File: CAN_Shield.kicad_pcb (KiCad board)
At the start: 2 copper layers, 65 x 56.5 mm, 22 parts, among them J1 GPIO, J2 KF128-2.54-4P, U1 MX128-5.08-09P-GN01-CU-Y-A, U2 MCP2515T-I/SO, U4 SN65HVD230DR, X1 X322516MLB4SI

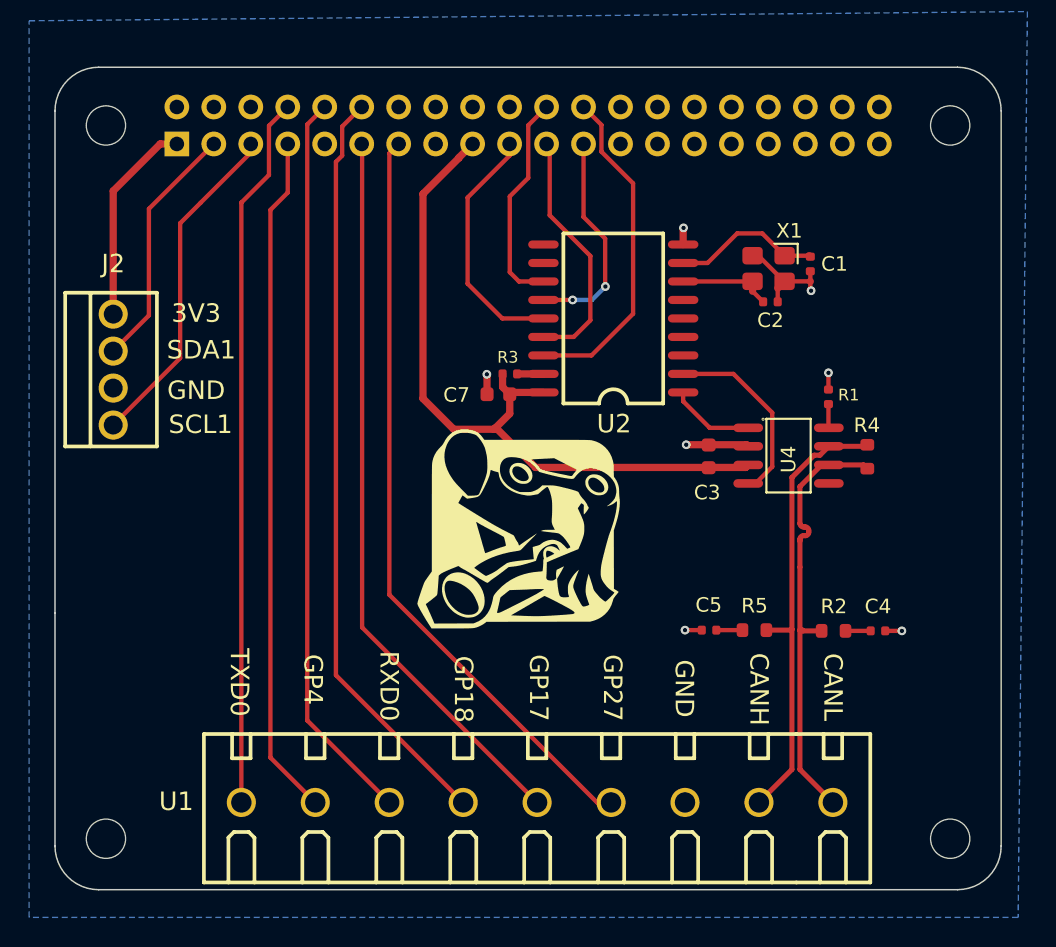
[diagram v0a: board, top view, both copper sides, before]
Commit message: finished schematics and layout for 3 terminal block except CAN
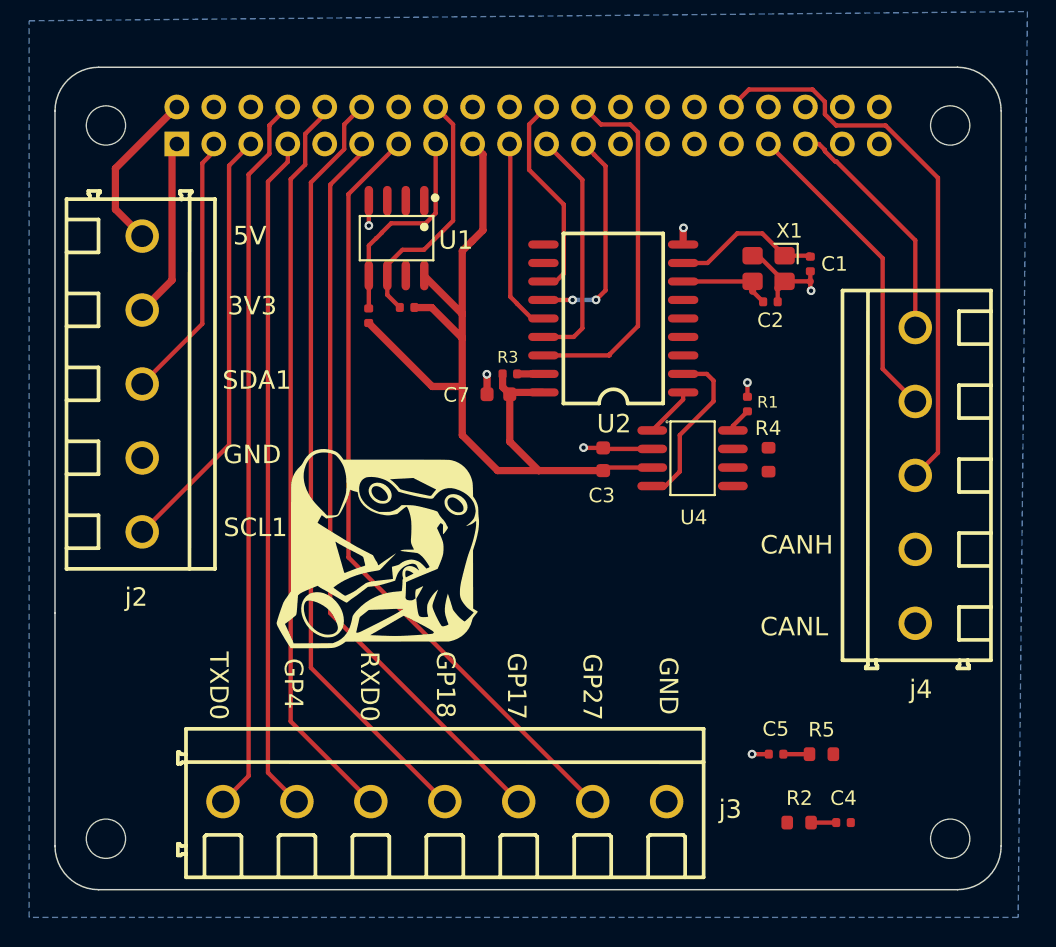
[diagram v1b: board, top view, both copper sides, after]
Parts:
- removed J2: KF128-2.54-4P, ImportFP:CONN-TH_4P-P2.54_KF128-2.54-4P
- added R6: 4.7kΩ, PCM_JLCPCB:R_0402, F.Cu at (124.2, 60.0)
- added R7: 4.7kΩ, PCM_JLCPCB:R_0402, F.Cu at (121.5, 60.6)
- added j2: DB128V-5.08-5P-GN-S, ImportFP:CONN-TH_5P-P5.08_DIBO_DB128V-5.08-5P-GN-S, F.Cu at (106.0, 65.3)
- added j3: DB128V-5.08-7P-GN-S, ImportFP:CONN-TH_7P-P5.08_DIBO_DB128V-5.08-7P-GN-S, F.Cu at (126.8, 94.0)
- added j4: DB128V-5.08-5P-GN-S, ImportFP:CONN-TH_5P-P5.08_DIBO_DB128V-5.08-5P-GN-S, F.Cu at (159.1, 71.5)
- U1: value MX128-5.08-09P-GN01-CU-Y-A -> ATECC608A-SSHDA-T; footprint ImportFP:CONN-TH_9P-P5.08_MX128-5.08-09P-GN01-CU-Y-A -> ImportFP:MICROCHIP ATECC608A-SSHDA-T
- moved U1 40.0 mm to (123.5, 55.2), turned to 180 degrees
- moved C4 13.4 mm to (154.2, 95.4)
- moved R2 13.4 mm to (151.1, 95.4)
- moved G*** 9.77 mm to (121.9, 76.5)
- moved C5 9.69 mm to (149.5, 90.7)
- moved R5 9.69 mm to (152.7, 90.7)
- moved C3 7.25 mm to (137.7, 70.4)
- moved R4 6.79 mm to (149.0, 70.5)
- moved U4 6.60 mm to (143.8, 70.4)
- moved R1 5.59 mm to (147.6, 66.6)
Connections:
- U1 pad 1: /GPIO14/TXD0 -> unconnected-(U1-NC-Pad1)
- U1 pad 2: /GPIO4/GPCLK0 -> unconnected-(U1-NC-Pad2)
- U1 pad 3: /GPIO15/RXD0 -> unconnected-(U1-NC-Pad3)
- U1 pad 4: /GPIO18/PCM.CLK -> GND
- U1 pad 5: /GPIO17 -> /GPIO22
- U1 pad 6: /GPIO27 -> /GPIO23
- U1 pad 7: GND -> unconnected-(U1-NC-Pad7)
- U1 pad 8: /CAN_D+ -> +3V3
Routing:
- net /GPIO12/PWM0: track 0.00 -> 38.8 mm
- net /CAN_D+: track 31.2 -> 0.04 mm
- net /CAN_D-: track 30.3 -> 0.00 mm
- net /GPIO13/PWM1: track 0.00 -> 21.9 mm
- net /GPIO23: track 0.00 -> 17.4 mm
- net /GPIO19/PCM.FS: track 0.00 -> 16.3 mm
- net /GPIO22: track 0.62 -> 15.2 mm
- net +5V: track 0.00 -> 11.4 mm
- net +3V3: track 64.2 -> 73.6 mm
- net /GPIO3/SCL1: track 23.2 -> 30.3 mm
- net /GPIO10/SPI0.MOSI: track 17.0 -> 13.4 mm
- net /GPIO8/SPI0.CE0: track 23.0 -> 25.1 mm
- net /TXCAN: track 5.83 -> 4.14 mm
- net /GPIO2/SDA1: track 17.1 -> 18.5 mm
- net /RXCAN: track 13.1 -> 11.8 mm
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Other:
- board text added: "5V"

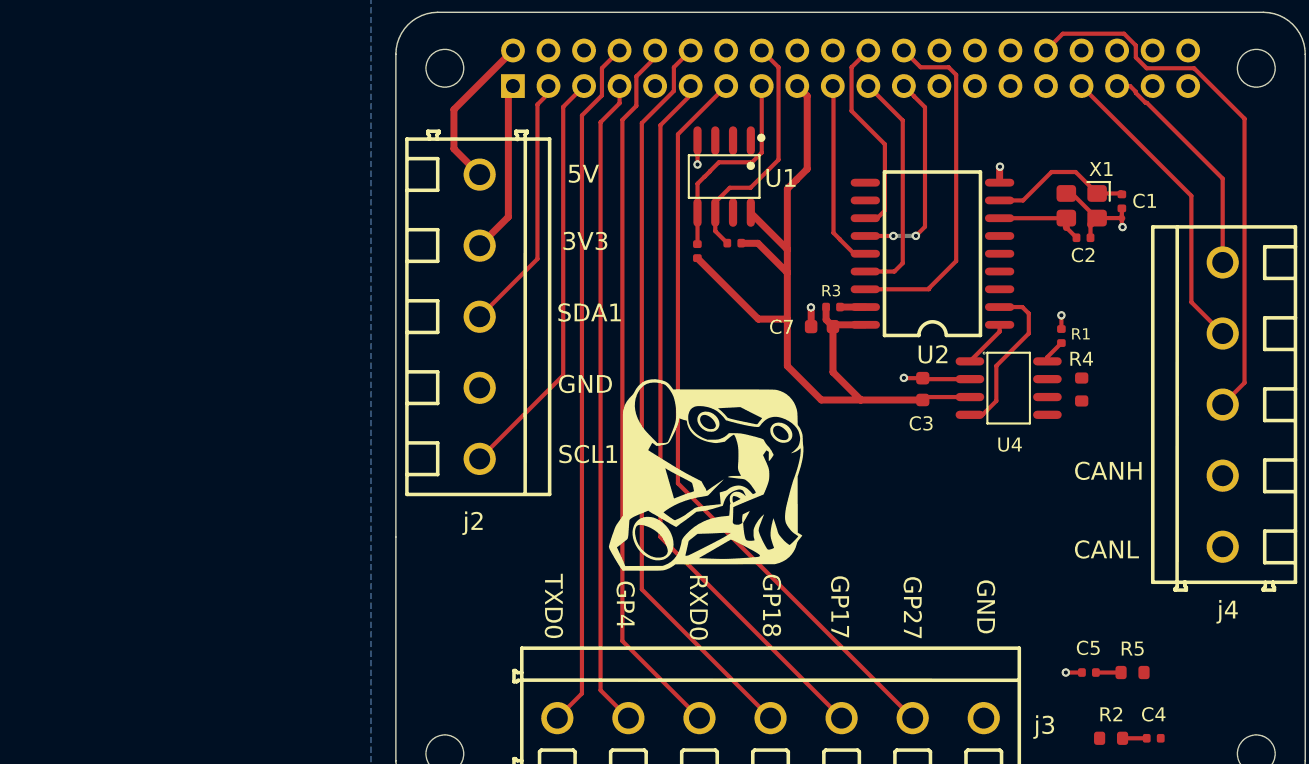
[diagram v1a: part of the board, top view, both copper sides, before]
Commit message: fix atecc608 silkscreen on pad (both lib and pcb editor) and adjust TxRx can distance
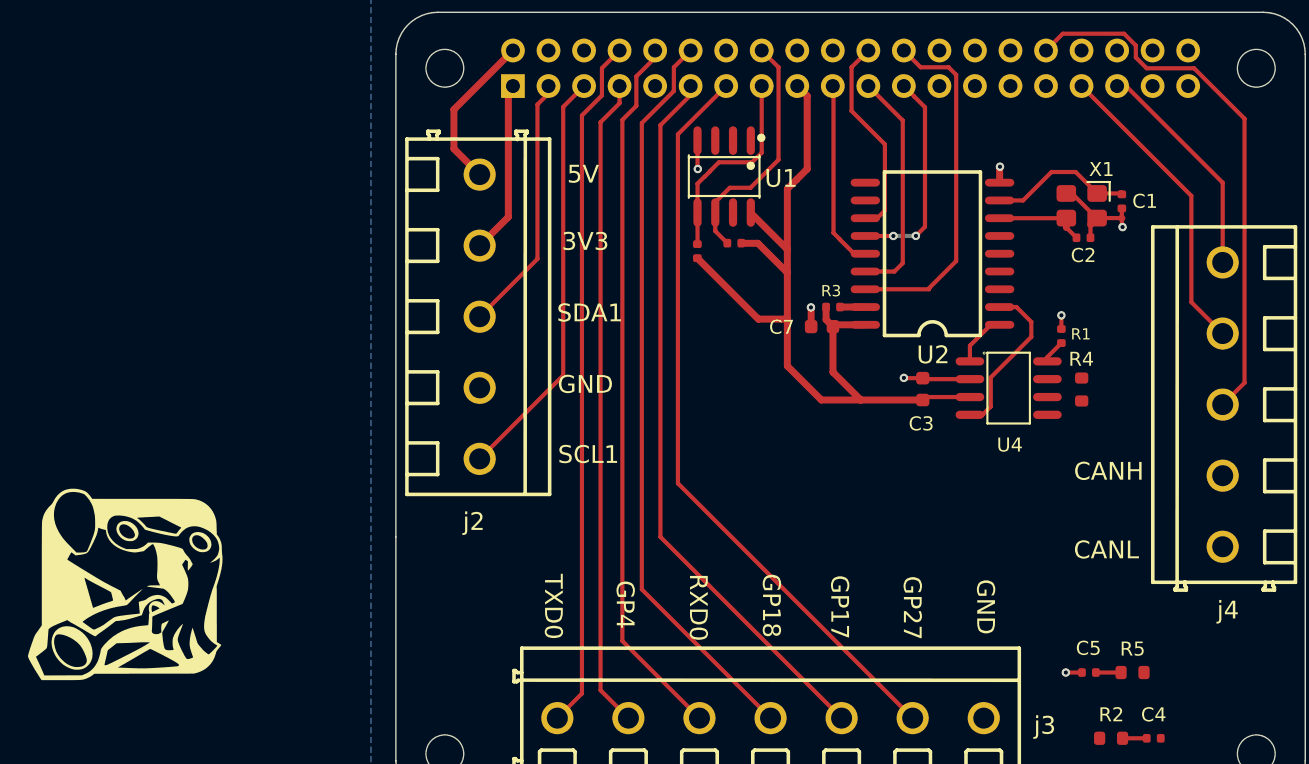
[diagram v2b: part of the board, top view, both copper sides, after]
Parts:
- moved G*** 42.3 mm to (80.4, 84.4)

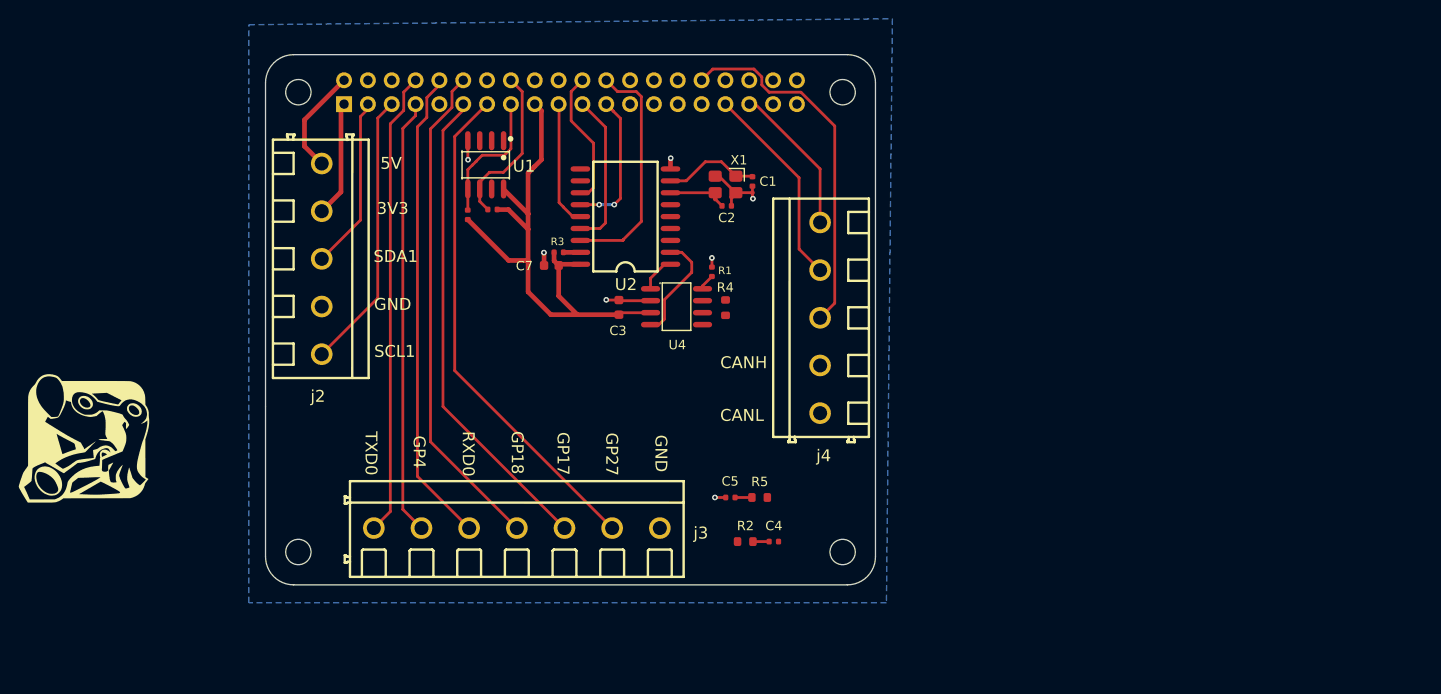
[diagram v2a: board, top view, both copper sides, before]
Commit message: add more pin for right terminal block (unfinished import footprint and arrangement with unfinished schematics and layout)
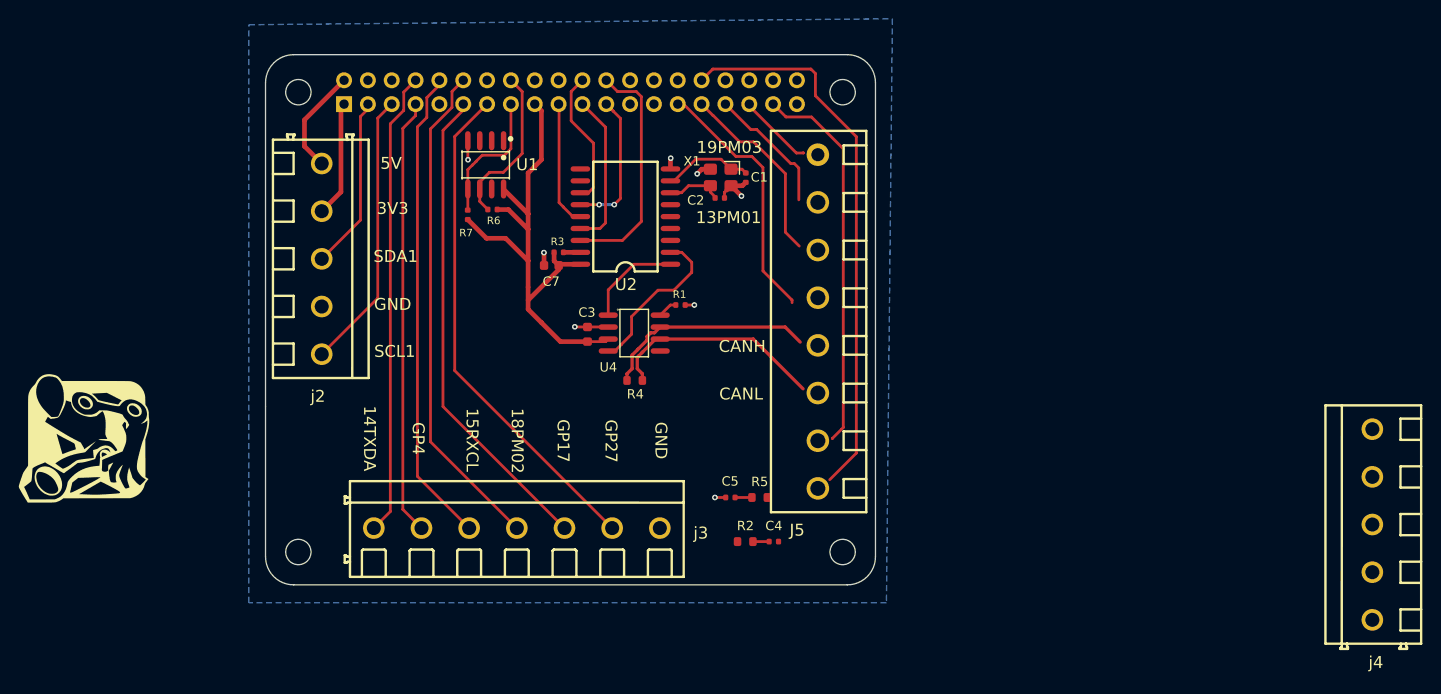
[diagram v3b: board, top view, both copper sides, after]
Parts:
- added J5: DB128V-5.08-8P-GN-S, ImportFP:CONN-TH_8P-P5.08_DB128V-5.08-8P-GN-S, F.Cu at (158.9, 71.9)
- moved j4 62.8 mm to (217.9, 93.6)
- moved R4 12.4 mm to (139.3, 78.2), turned to 180 degrees
- moved U4 5.31 mm to (139.3, 73.2)
- moved R1 4.87 mm to (144.2, 70.2), turned to 0 degrees
- moved C3 4.41 mm to (134.3, 73.3)
- moved C2 1.12 mm to (148.4, 58.8)
- moved X1 0.90 mm to (148.5, 56.6)
- moved C1 0.82 mm to (151.2, 56.6)
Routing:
- net /GPIO26: track 0.00 -> 40.8 mm
- net /GPIO5: track 0.00 -> 27.6 mm
- net /CAN_D-: track 0.00 -> 23.4 mm
- net /CAN_D+: track 0.04 -> 23.0 mm
- net /GPIO6: track 0.00 -> 20.3 mm
- net /GPIO12/PWM0: track 38.8 -> 59.1 mm
- net /GPIO13/PWM1: track 21.9 -> 14.0 mm
- net /GPIO19/PCM.FS: track 16.1 -> 8.70 mm
- net /TXCAN: track 3.86 -> 11.1 mm
- net /RXCAN: track 11.7 -> 18.0 mm
- net +3V3: track 73.6 -> 70.8 mm
- net GND: track 19.2 -> 17.9 mm, vias 7 -> 8
- net /OSC1: track 10.2 -> 9.68 mm
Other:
- board text added: "13PM01"
- board text added: "14TXDA"
- board text added: "15RXCL"
- board text added: "18PM02"
- board text added: "19PM03"
- board text removed: "GP18"
- board text removed: "RXD0"
- board text removed: "TXD0"

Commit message: increase terminal block and 40 pin header spacing for easy soldering, also use DB-7P instead of 8 pin, add ESD diode for CAN
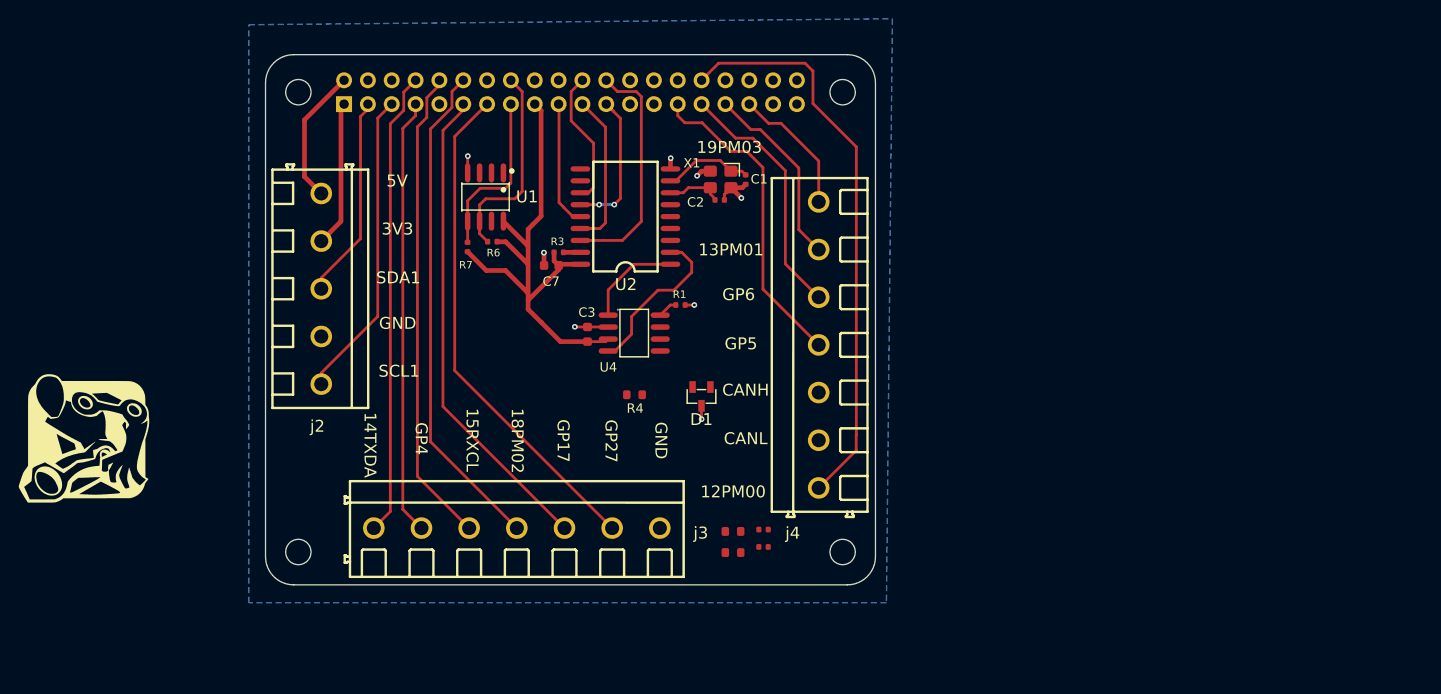
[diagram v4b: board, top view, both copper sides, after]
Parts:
- removed J5: DB128V-5.08-8P-GN-S, ImportFP:CONN-TH_8P-P5.08_DB128V-5.08-8P-GN-S
- added D1: ESD2CANFD24DBZR, ImportFP:TI ESD2CANFD24DBZR, F.Cu at (146.5, 79.9)
- j4: value DB128V-5.08-5P-GN-S -> DB128V-5.08-7P-GN-S; footprint ImportFP:CONN-TH_5P-P5.08_DIBO_DB128V-5.08-5P-GN-S -> ImportFP:CONN-TH_7P-P5.08_DIBO_DB128V-5.08-7P-GN-S
- moved j4 62.0 mm to (158.9, 74.4)
- moved R5 6.52 mm to (149.8, 96.6), turned to 0 degrees
- moved C5 6.34 mm to (153.1, 96.0), turned to 0 degrees
- moved R6 3.43 mm to (124.2, 63.4)
- moved R7 3.43 mm to (121.5, 64.0)
- moved U1 3.43 mm to (123.4, 58.7)
- moved j2 3.19 mm to (105.9, 68.5)
- moved R2 1.69 mm to (149.8, 94.3)
- moved C4 1.69 mm to (153.1, 94.1)
- moved R4 1.52 mm to (139.3, 79.7)
- moved C1 0.21 mm to (151.2, 56.8)
- moved X1 0.21 mm to (148.5, 56.8)
- moved C2 0.21 mm to (148.4, 59.0)
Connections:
- j4 pad 1: /CAN_D- -> /GPIO12/PWM0
- j4 pad 2: /CAN_D+ -> /CAN_D-
- j4 pad 3: /GPIO12/PWM0 -> /CAN_D+
- j4 pad 4: /GPIO13/PWM1 -> /GPIO5
- j4 pad 5: /GPIO19/PCM.FS -> /GPIO6
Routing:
- net /GPIO26: track 40.8 -> 0.00 mm
- net /CAN_D-: track 23.4 -> 0.00 mm
- net /CAN_D+: track 23.0 -> 0.00 mm
- net /GPIO6: track 20.3 -> 26.8 mm
- net /GPIO5: track 27.6 -> 34.0 mm
- net /GPIO19/PCM.FS: track 8.70 -> 14.9 mm
- net /GPIO13/PWM1: track 14.0 -> 20.2 mm
- net /GPIO3/SCL1: track 30.3 -> 34.8 mm
- net /GPIO23: track 17.4 -> 21.1 mm
- net /GPIO22: track 15.2 -> 18.8 mm
- net /GPIO2/SDA1: track 18.5 -> 21.7 mm
- net +3V3: track 70.8 -> 74.0 mm
- net +5V: track 11.4 -> 14.5 mm
- net /GPIO12/PWM0: track 59.1 -> 61.0 mm
- net Net-(C5-Pad1): track 1.80 -> 0.00 mm
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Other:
- board text added: "12PM00"
- board text added: "GP5"
- board text added: "GP6"

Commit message: finished can split termination and TVS diode layout
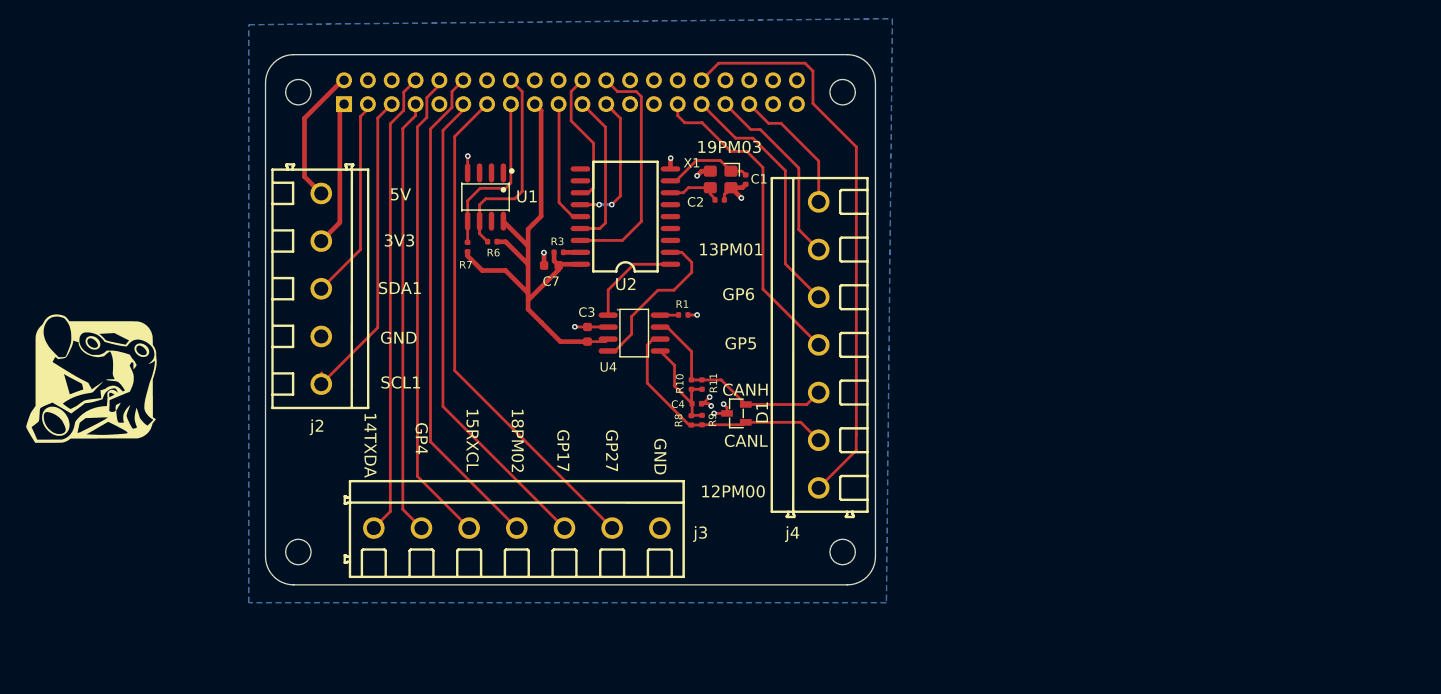
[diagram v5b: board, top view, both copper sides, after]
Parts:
- removed C5: 470pF, PCM_JLCPCB:C_0402
- removed R2, R4, R5: 120Ω, PCM_JLCPCB:R_0603
- added R10: 120Ω, PCM_JLCPCB:R_0402, F.Cu at (145.4, 78.7)
- added R11: 120Ω, PCM_JLCPCB:R_0402, F.Cu at (146.5, 78.7)
- added R8: 120Ω, PCM_JLCPCB:R_0402, F.Cu at (145.4, 82.5)
- added R9: 120Ω, PCM_JLCPCB:R_0402, F.Cu at (146.5, 82.4)
- moved C4 15.2 mm to (146.0, 80.7)
- moved G*** 6.42 mm to (81.2, 78.0)
- moved D1 4.14 mm to (150.2, 81.7), turned to 90 degrees
- moved R1 1.10 mm to (144.5, 71.2)
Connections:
- C4 pad 1: Net-(C4-Pad1) -> Net-(U4-VREF)
- D1 pad 1: /CAN_D+ -> /CAN_D-
- D1 pad 2: /CAN_D- -> /CAN_D+
- U4 pad 5: unconnected-(U4-VREF-Pad5) -> Net-(U4-VREF)
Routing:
- net /CAN_D-: track 0.00 -> 26.7 mm
- net /CAN_D+: track 0.00 -> 22.6 mm
- net Net-(U4-VREF): track 0.00 -> 12.2 mm
- net GND: track 18.0 -> 21.3 mm, vias 8 -> 11
